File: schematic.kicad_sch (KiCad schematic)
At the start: 0 parts

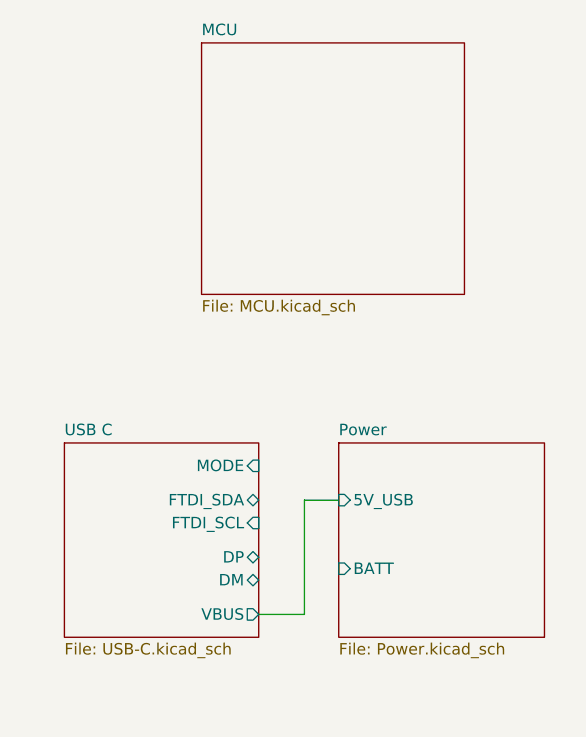
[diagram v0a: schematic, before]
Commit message: Added power schematic
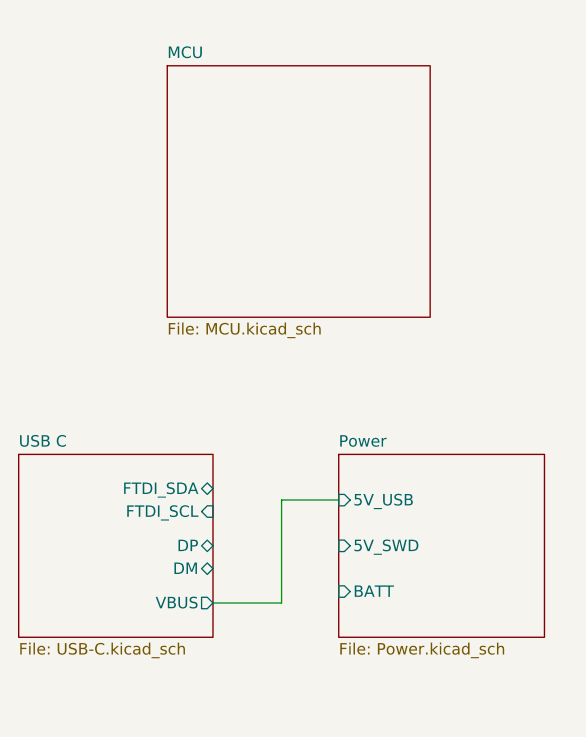
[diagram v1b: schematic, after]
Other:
- sheet Power ports: added 5V_SWD; removed none
- sheet USB C ports: added none; removed MODE
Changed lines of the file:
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@@
 	(wire
 		(pts
-			(xy 142.24 127) (xy 142.24 114.3)
+			(xy 139.7 125.73) (xy 139.7 114.3)
 		)
 		(stroke
@@
 	(wire
 		(pts
-			(xy 137.16 127) (xy 142.24 127)
+			(xy 132.08 125.73) (xy 139.7 125.73)
 		)
 		(stroke
@@
 	(wire
 		(pts
-			(xy 142.24 114.3) (xy 146.05 114.3)
+			(xy 139.7 114.3) (xy 146.05 114.3)
 		)
 		(stroke
@@
 				)
 			)
-			(table_cell "MCU\nEERAM\nTRANSCEIVER"
+			(table_cell "MCU\nEERAM\nTRANSCEIVER\nANALOG SWITCHES"
 				(exclude_from_sim no)
 				(at 111.76 38.1 0)
@@
 				)
 			)
-			(table_cell ""
+			(table_cell "USB SWITCH\nFTDI CHIP\nCONNECTOR"
 				(exclude_from_sim no)
 				(at 132.08 38.1 0)
@@
 				)
 			)
-			(table_cell ""
+			(table_cell "BUCK\nLDO\nPOWER SWITCH"
 				(exclude_from_sim no)
 				(at 152.4 38.1 0)
@@
 	)
 	(sheet
-		(at 115.57 107.95)
-		(size 21.59 21.59)
+		(at 110.49 109.22)
+		(size 21.59 20.32)
 		(exclude_from_sim no)
 		(in_bom yes)
@@
 		)
 		(property "Sheetname" "USB C"
-			(at 115.57 107.2384 0)
+			(at 110.49 108.5084 0)
 			(show_name no)
 			(do_not_autoplace no)
@@
 		)
 		(property "Sheetfile" "USB-C.kicad_sch"
-			(at 115.57 130.1246 0)
+			(at 110.49 130.1246 0)
 			(show_name no)
 			(do_not_autoplace no)
@@
 		)
 		(pin "DM" bidirectional
-			(at 137.16 123.19 0)
+			(at 132.08 121.92 0)
 			(effects
 				(font
@@
 		)
 		(pin "DP" bidirectional
-			(at 137.16 120.65 0)
+			(at 132.08 119.38 0)
 			(effects
 				(font
@@
 		)
 		(pin "FTDI_SCL" input
-			(at 137.16 116.84 0)
+			(at 132.08 115.57 0)
 			(effects
 				(font
@@
 		)
 		(pin "FTDI_SDA" bidirectional
-			(at 137.16 114.3 0)
-			(effects
-				(font
-					(size 1.27 1.27)
-				)
-				(justify right)
-			)
-		)
-		(pin "MODE" input
-			(at 137.16 110.49 0)
+			(at 132.08 113.03 0)
 			(effects
 				(font
@@
 		)
 		(pin "VBUS" output
-			(at 137.16 127 0)
+			(at 132.08 125.73 0)
 			(effects
 				(font
@@
 	)
 	(sheet
-		(at 146.05 107.95)
-		(size 22.86 21.59)
+		(at 146.05 109.22)
+		(size 22.86 20.32)
 		(exclude_from_sim no)
 		(in_bom yes)
@@
 		)
 		(property "Sheetname" "Power"
-			(at 146.05 107.2384 0)
+			(at 146.05 108.5084 0)
 			(show_name no)
 			(do_not_autoplace no)
@@
 		)
 		(pin "BATT" input
-			(at 146.05 121.92 180)
+			(at 146.05 124.46 180)
+			(effects
+				(font
+					(size 1.27 1.27)
+				)
+				(justify left)
+			)
+		)
+		(pin "5V_SWD" input
+			(at 146.05 119.38 180)
 			(effects
 				(font
@@
 	)
 	(sheet
-		(at 130.81 63.5)
+		(at 127 66.04)
 		(size 29.21 27.94)
 		(exclude_from_sim no)
@@
 		)
 		(property "Sheetname" "MCU"
-			(at 130.81 62.7884 0)
+			(at 127 65.3284 0)
 			(show_name no)
 			(do_not_autoplace no)
@@
 		)
 		(property "Sheetfile" "MCU.kicad_sch"
-			(at 130.81 92.0246 0)
-			(show_name no)
-			(do_not_autoplace no)
+			(at 127 94.5646 0)
+			(show_name no)
+			(do_not_autoplace no)

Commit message: Added todos
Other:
- sheet MCU ports: added DM, DP, MODE, SCL, SDA; removed none
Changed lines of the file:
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@@
+			)
+		)
+		(pin "DM" input
+			(at 127 87.63 180)
+			(effects
+				(font
+					(size 1.27 1.27)
+				)
+				(justify left)
+			)
+		)
+		(pin "DP" input
+			(at 127 83.82 180)
+			(effects
+				(font
+					(size 1.27 1.27)
+				)
+				(justify left)
+			)
+		)
+		(pin "MODE" input
+			(at 127 78.74 180)
+			(effects
+				(font
+					(size 1.27 1.27)
+				)
+				(justify left)
+			)
+		)
+		(pin "SCL" input
+			(at 127 74.93 180)
+			(effects
+				(font
+					(size 1.27 1.27)
+				)
+				(justify left)
+			)
+		)
+		(pin "SDA" input
+			(at 127 71.12 180)
+			(effects
+				(font
+					(size 1.27 1.27)
+				)
+				(justify left)
 			)
 		)

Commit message: Started PCB
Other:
- sheet USB C ports: added FT_KEEP_AWAKE, FT_PWREN; removed none
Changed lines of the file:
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@@
 	(sheet
 		(at 110.49 109.22)
-		(size 21.59 20.32)
+		(size 21.59 26.67)
 		(exclude_from_sim no)
 		(in_bom yes)
@@
 		)
 		(property "Sheetfile" "USB-C.kicad_sch"
-			(at 110.49 130.1246 0)
+			(at 110.49 136.4746 0)
 			(show_name no)
 			(do_not_autoplace no)
@@
 			(effects
 				(font
+					(size 1.27 1.27)
+				)
+				(justify right)
+			)
+		)
+		(pin "FT_KEEP_AWAKE" input
+			(at 132.08 129.54 0)
+			(effects
+				(font
+					(size 1.27 1.27)
+				)
+				(justify right)
+			)
+		)
+		(pin "FT_PWREN" output
+			(at 132.08 132.08 0)
+			(effects
+				(font
